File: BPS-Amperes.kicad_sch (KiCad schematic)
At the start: 32 parts, among them J1 Conn_02x10_Odd_Even, J2 ShuntConn, U1 INA186A3IDDFT, U2 OPA2196, U3 LTC2315, U4 REF1930AIDDCT

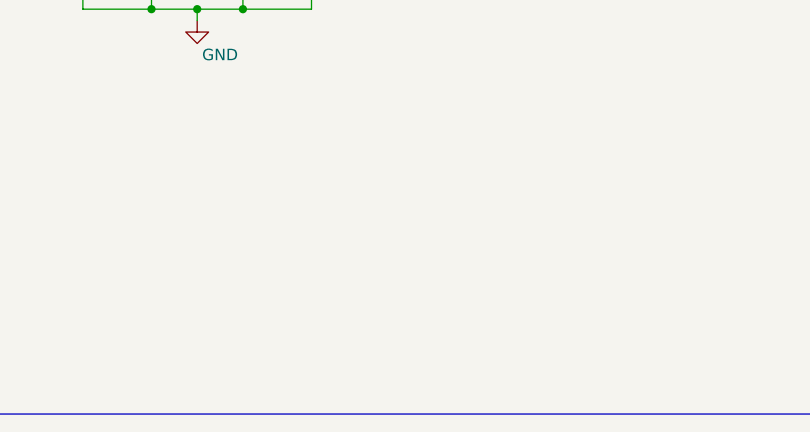
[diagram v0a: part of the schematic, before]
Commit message: Added datasheet links
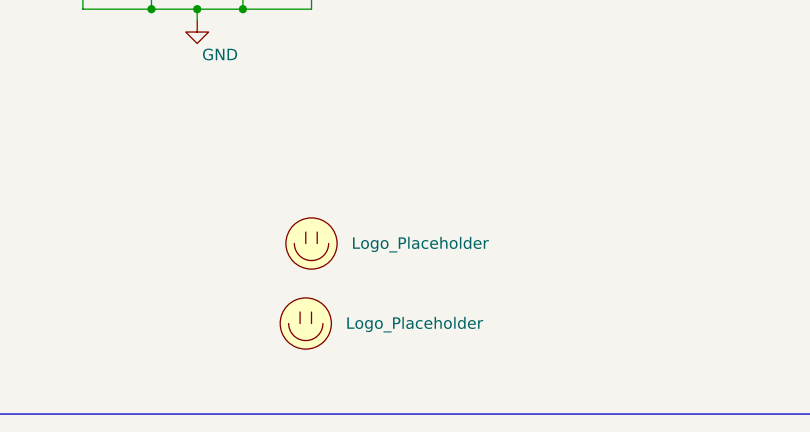
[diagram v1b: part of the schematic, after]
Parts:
- added LOGO1, LOGO2: Logo_Placeholder, symbol utsvt-misc:Logo_Placeholder
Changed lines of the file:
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@@
       (effects (font (size 1.27 1.27)) hide)
     )
-    (property "Datasheet" "~" (at 133.985 86.36 0)
+    (property "Datasheet" "https://www.mouser.com/ProductDetail/KEMET/C0805C470JAGACAUTO?qs=f0OuG6fVDNYyqynuVfVSSA%3D%3D" (at 133.985 86.36 0)
       (effects (font (size 1.27 1.27)) hide)
     )
@@
       (effects (font (size 1.27 1.27)) hide)
     )
-    (property "Datasheet" "https://www.mouser.com/ProductDetail/KEMET/C0805C105K5PACTU?qs=mYAa4mSiDJyTAfAbrHf%2FRg%3D%3D" (at 90.17 149.225 0)
+    (property "Datasheet" "https://www.mouser.com/ProductDetail/80-C0805C105K5P" (at 90.17 149.225 0)
       (effects (font (size 1.27 1.27)) hide)
     )
@@
       (effects (font (size 1.27 1.27)) hide)
     )
-    (property "Datasheet" "~" (at 53.975 40.64 0)
+    (property "Datasheet" "https://www.mouser.com/ProductDetail/Vishay-Dale/CRCW08051K20FKEA?qs=sGAEpiMZZMvdGkrng054txEw7b1YnvGupB6U2wYbbWU%3D" (at 53.975 40.64 0)
       (effects (font (size 1.27 1.27)) hide)
     )
@@
       (effects (font (size 1.27 1.27)) hide)
     )
-    (property "Datasheet" "" (at 45.085 76.2 0)
+    (property "Datasheet" "https://www.mouser.com/ProductDetail/Texas-Instruments/INA186A3IDDFT?qs=wnTfsH77Xs4bZM5PeQ9%252BVw%3D%3D" (at 45.085 76.2 0)
       (effects (font (size 1.27 1.27)) hide)
     )
@@
       (effects (font (size 1.27 1.27)) hide)
     )
-    (property "Datasheet" "https://tools.molex.com/pdm_docs/sd/533072071_sd.pdf" (at 246.38 35.56 0)
+    (property "Datasheet" "https://www.mouser.com/ProductDetail/Molex/53307-2071?qs=88IJkhYWEX1NdBDaDFqnDg%3D%3D" (at 246.38 35.56 0)
       (effects (font (size 1.27 1.27)) hide)
     )
@@
       (effects (font (size 1.27 1.27)) hide)
     )
-    (property "Datasheet" "~" (at 166.37 58.42 0)
+    (property "Datasheet" "https://www.mouser.com/ProductDetail/KEMET/C0805C225K5RACAUTO?qs=HBWAp0VN4RhaI2JFGdfu4w%3D%3D" (at 166.37 58.42 0)
       (effects (font (size 1.27 1.27)) hide)
     )
@@
       (effects (font (size 1.27 1.27)) hide)
     )
-    (property "Datasheet" "https://www.mouser.com/ProductDetail/KEMET/C0805C105K5PACTU?qs=mYAa4mSiDJyTAfAbrHf%2FRg%3D%3D" (at 107.95 149.225 0)
+    (property "Datasheet" "https://www.mouser.com/ProductDetail/80-C0805C105K5P" (at 107.95 149.225 0)
       (effects (font (size 1.27 1.27)) hide)
     )
@@
       (effects (font (size 1.27 1.27)) hide)
     )
-    (property "Datasheet" "~" (at 76.835 76.2 0)
+    (property "Datasheet" "https://www.mouser.com/ProductDetail/Vishay-Dale/CRCW080510K0FKEAC?qs=E3Y5ESvWgWORadmUijPtxQ%3D%3D" (at 76.835 76.2 0)
       (effects (font (size 1.27 1.27)) hide)
     )
@@
       (effects (font (size 1.27 1.27)) hide)
     )
-    (property "Datasheet" "~" (at 61.595 41.91 0)
+    (property "Datasheet" "https://www.mouser.com/ProductDetail/KEMET/C0805C225K5RACAUTO?qs=HBWAp0VN4RhaI2JFGdfu4w%3D%3D" (at 61.595 41.91 0)
       (effects (font (size 1.27 1.27)) hide)
     )
@@
       (effects (font (size 1.27 1.27)) hide)
     )
-    (property "Datasheet" "" (at 73.66 141.605 0)
+    (property "Datasheet" "https://www.mouser.com/ProductDetail/Texas-Instruments/REF1930AIDDCT?qs=asCBFxFfL1QmJsJdAfkt%252BQ%3D%3D" (at 73.66 141.605 0)
       (effects (font (size 1.27 1.27)) hide)
     )
@@
       (effects (font (size 1.27 1.27)) hide)
     )
-    (property "Datasheet" "http://www.ti.com/lit/ds/symlink/opa4196.pdf" (at 111.125 69.85 0)
+    (property "Datasheet" "https://www.mouser.com/ProductDetail/Texas-Instruments/OPA2196ID?qs=EU6FO9ffTwckiWI91ID8yA%3D%3D" (at 111.125 69.85 0)
       (effects (font (size 1.27 1.27)) hide)
     )
@@
       (effects (font (size 1.27 1.27)) hide)
     )
-    (property "Datasheet" "" (at 150.495 74.93 0)
+    (property "Datasheet" "https://www.mouser.com/ProductDetail/Analog-Devices/LTC2315ITS8-12TRMPBF?qs=hVkxg5c3xu9zBLlrgAxfpg%3D%3D" (at 150.495 74.93 0)
       (effects (font (size 1.27 1.27)) hide)
     )
@@
       (effects (font (size 1.27 1.27)) hide)
     )
-    (property "Datasheet" "~" (at 82.55 82.55 0)
+    (property "Datasheet" "https://www.mouser.com/ProductDetail/KEMET/C0805C474K3RAC?qs=1r5zKhvYIsjK11w1M%252BoEzg%3D%3D" (at 82.55 82.55 0)
       (effects (font (size 1.27 1.27)) hide)
     )
@@
       (effects (font (size 1.27 1.27)) hide)
     )
-    (property "Datasheet" "~" (at 132.08 55.88 0)
+    (property "Datasheet" "https://www.mouser.com/ProductDetail/KEMET/C0805C225K5RACAUTO?qs=HBWAp0VN4RhaI2JFGdfu4w%3D%3D" (at 132.08 55.88 0)
       (effects (font (size 1.27 1.27)) hide)
     )
@@
       (effects (font (size 1.27 1.27)) hide)
     )
-    (property "Datasheet" "~" (at 53.975 43.18 0)
+    (property "Datasheet" "https://www.mouser.com/ProductDetail/Vishay-Dale/CRCW08051K20FKEA?qs=sGAEpiMZZMvdGkrng054txEw7b1YnvGupB6U2wYbbWU%3D" (at 53.975 43.18 0)
       (effects (font (size 1.27 1.27)) hide)
     )
@@
       (effects (font (size 1.27 1.27)) hide)
     )
-    (property "Datasheet" "~" (at 128.905 78.74 0)
+    (property "Datasheet" "https://www.mouser.com/ProductDetail/Vishay-Beyschlag/MCU08050C4999FP500?qs=SrWqTHi7C4DOMypgR8IlmQ%3D%3D" (at 128.905 78.74 0)
       (effects (font (size 1.27 1.27)) hide)
     )
@@
       (effects (font (size 1.27 1.27)) hide)
     )
-    (property "Datasheet" "http://www.ti.com/lit/ds/symlink/opa4196.pdf" (at 93.345 69.85 0)
+    (property "Datasheet" "https://www.mouser.com/ProductDetail/Texas-Instruments/OPA2196ID?qs=EU6FO9ffTwckiWI91ID8yA%3D%3D" (at 93.345 69.85 0)
       (effects (font (size 1.27 1.27)) hide)
     )
@@
       (effects (font (size 1.27 1.27)) hide)
     )
-    (property "Datasheet" "~" (at 65.405 76.2 0)
+    (property "Datasheet" "https://www.mouser.com/ProductDetail/Vishay-Dale/CRCW080510K0FKEAC?qs=E3Y5ESvWgWORadmUijPtxQ%3D%3D" (at 65.405 76.2 0)
       (effects (font (size 1.27 1.27)) hide)
     )
@@
     )
   )
+  (symbol (lib_id "utsvt-misc:Logo_Placeholder") (at 114.935 187.96 0) (unit 1)
+    (in_bom yes) (on_board yes) (dnp no) (fields_autoplaced)
+    (property "Reference" "LOGO1" (at 114.935 184.15 0)
+      (effects (font (size 1.27 1.27)) hide)
+    )
+    (property "Value" "Logo_Placeholder" (at 119.38 187.96 0)
+      (effects (font (size 1.27 1.27)) (justify left))
+    )
+    (property "Footprint" "" (at 114.935 186.055 0)
+      (effects (font (size 1.27 1.27)) hide)
+    )
+    (property "Datasheet" "" (at 114.935 186.055 0)
+      (effects (font (size 1.27 1.27)) hide)
+    )
+    (instances
+      (project "BPS-Amperes"
+        (path "/637f68f0-cb9c-412a-8573-5d8e7ef6d8a2"
+          (reference "LOGO1") (unit 1)
+        )
+      )
+    )
+  )
   (symbol (lib_id "Connector:TestPoint") (at 97.79 139.065 0) (unit 1)
     (in_bom yes) (on_board yes) (dnp no)
@@
     )
   )
+  (symbol (lib_id "utsvt-misc:Logo_Placeholder") (at 115.57 179.07 0) (unit 1)
+    (in_bom yes) (on_board yes) (dnp no) (fields_autoplaced)
+    (property "Reference" "LOGO2" (at 115.57 175.26 0)
+      (effects (font (size 1.27 1.27)) hide)
+    )
+    (property "Value" "Logo_Placeholder" (at 120.015 179.07 0)
+      (effects (font (size 1.27 1.27)) (justify left))
+    )
+    (property "Footprint" "" (at 115.57 177.165 0)
+      (effects (font (size 1.27 1.27)) hide)
+    )
+    (property "Datasheet" "" (at 115.57 177.165 0)
+      (effects (font (size 1.27 1.27)) hide)
+    )
+    (instances
+      (project "BPS-Amperes"
+        (path "/637f68f0-cb9c-412a-8573-5d8e7ef6d8a2"
+          (reference "LOGO2") (unit 1)
+        )
+      )
+    )
+  )
   (symbol (lib_id "Device:FerriteBead_Small") (at 86.36 141.605 90) (unit 1)
     (in_bom yes) (on_board yes) (dnp no)
@@
       (effects (font (size 1.27 1.27)) hide)
     )
-    (property "Datasheet" "https://www.mouser.com/ProductDetail/KEMET/C0805C105K5PACTU?qs=mYAa4mSiDJyTAfAbrHf%2FRg%3D%3D" (at 71.755 69.85 0)
+    (property "Datasheet" "https://www.mouser.com/ProductDetail/80-C0805C105K5P" (at 71.755 69.85 0)
       (effects (font (size 1.27 1.27)) hide)
     )
@@
       (effects (font (size 1.27 1.27)) hide)
     )
-    (property "Datasheet" "http://www.ti.com/lit/ds/symlink/opa4196.pdf" (at 113.665 68.58 0)
+    (property "Datasheet" "https://www.mouser.com/ProductDetail/Texas-Instruments/OPA2196ID?qs=EU6FO9ffTwckiWI91ID8yA%3D%3D" (at 113.665 68.58 0)
       (effects (font (size 1.27 1.27)) hide)
     )
@@
       (effects (font (size 1.27 1.27)) hide)
     )
-    (property "Datasheet" "https://www.mouser.com/ProductDetail/KEMET/C0805C105K5PACTU?qs=mYAa4mSiDJyTAfAbrHf%2FRg%3D%3D" (at 24.765 73.66 0)
+    (property "Datasheet" "https://www.mouser.com/ProductDetail/80-C0805C105K5P" (at 24.765 73.66 0)
       (effects (font (size 1.27 1.27)) hide)
     )
@@
       (effects (font (size 1.27 1.27)) hide)
     )
-    (property "Datasheet" "~" (at 139.7 55.88 0)
-      (effects (font (size 1.27 1.27)) hide)
-    )
+    (property "Datasheet" "https://www.mouser.com/ProductDetail/KEMET/C0805C225K5RACAUTO?qs=HBWAp0VN4RhaI2JFGdfu4w%3D%3D" (at 139.7 55.88 0)
+      (effects (font (size 1.27 1.27)) hide)
+    )

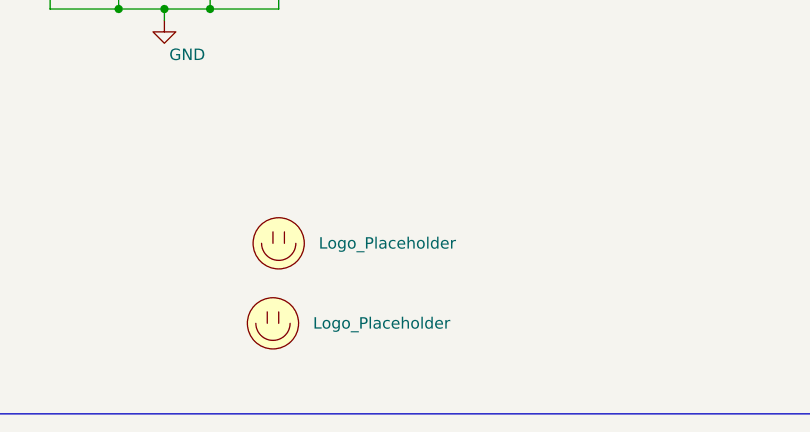
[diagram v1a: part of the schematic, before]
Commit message: Added Hallock and LHRs Logo
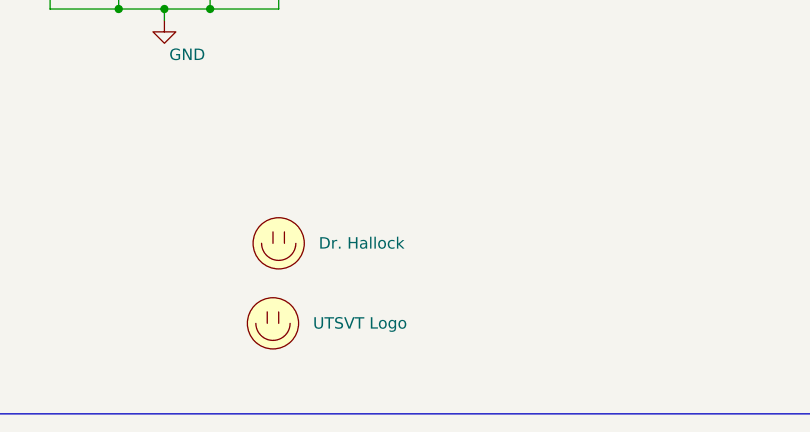
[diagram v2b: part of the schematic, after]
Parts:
- LOGO1: value Logo_Placeholder -> UTSVT Logo; footprint (none) -> UTSVT_Special:UTSVT_Logo_Symbol
- MiniHallock: renamed from LOGO2; value Logo_Placeholder -> Dr. Hallock; footprint (none) -> UTSVT_Special:Hallock_Image_Tiny
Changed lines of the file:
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@@
       (effects (font (size 1.27 1.27)) hide)
     )
-    (property "Value" "Logo_Placeholder" (at 119.38 187.96 0)
+    (property "Value" "UTSVT Logo" (at 119.38 187.96 0)
       (effects (font (size 1.27 1.27)) (justify left))
     )
-    (property "Footprint" "" (at 114.935 186.055 0)
+    (property "Footprint" "UTSVT_Special:UTSVT_Logo_Symbol" (at 114.935 186.055 0)
       (effects (font (size 1.27 1.27)) hide)
     )
@@
   (symbol (lib_id "utsvt-misc:Logo_Placeholder") (at 115.57 179.07 0) (unit 1)
     (in_bom yes) (on_board yes) (dnp no) (fields_autoplaced)
-    (property "Reference" "LOGO2" (at 115.57 175.26 0)
+    (property "Reference" "MiniHallock" (at 115.57 175.26 0)
       (effects (font (size 1.27 1.27)) hide)
     )
-    (property "Value" "Logo_Placeholder" (at 120.015 179.07 0)
+    (property "Value" "Dr. Hallock" (at 120.015 179.07 0)
       (effects (font (size 1.27 1.27)) (justify left))
     )
-    (property "Footprint" "" (at 115.57 177.165 0)
+    (property "Footprint" "UTSVT_Special:Hallock_Image_Tiny" (at 115.57 177.165 0)
       (effects (font (size 1.27 1.27)) hide)
     )
@@
       (project "BPS-Amperes"
         (path "/637f68f0-cb9c-412a-8573-5d8e7ef6d8a2"
-          (reference "LOGO2") (unit 1)
+          (reference "MiniHallock") (unit 1)
         )
       )
